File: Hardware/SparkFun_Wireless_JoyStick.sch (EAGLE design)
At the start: 75 parts, among them J7 CORTEX_DEBUGPTH, Q1 2.5A/30V, U1 JOYSTICKPTH, U2 JOYSTICKPTH, U3 74AHC1G125, U4 AP2112K-3.3V, U5 XBEE-2B3, U6 MAX1704X, U7 MCP73831, U8 ATSAMD21G-A, Y1 32.768kHz

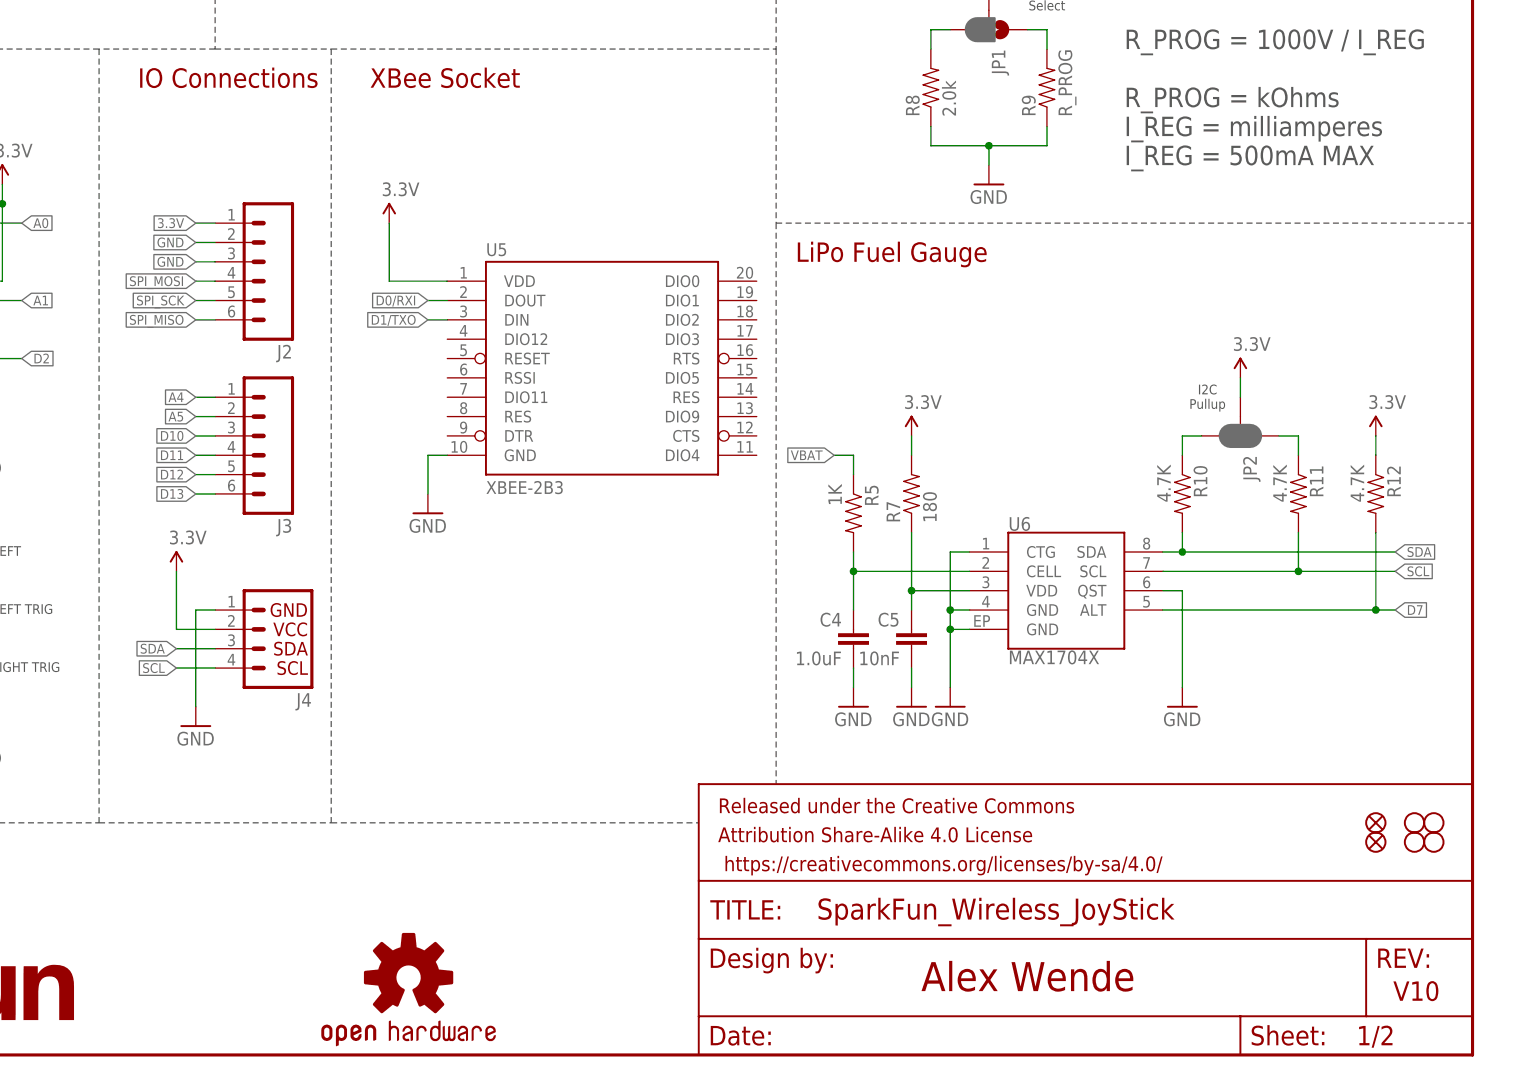
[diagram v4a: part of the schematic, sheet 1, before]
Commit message: QC Issues Fixed
- TX_LED and RX_LED nets are now all 0.006" width
- Version number changed to v01
- IO connections use 3.3V and GND symbols instead of net labels
- Replaced VBAT net label in LiPo Fuel Gauge with PWR symbol
- Inductor PROD_ID updated to match SKU in Sparkle
- Moved JTAG test points to bottom copper
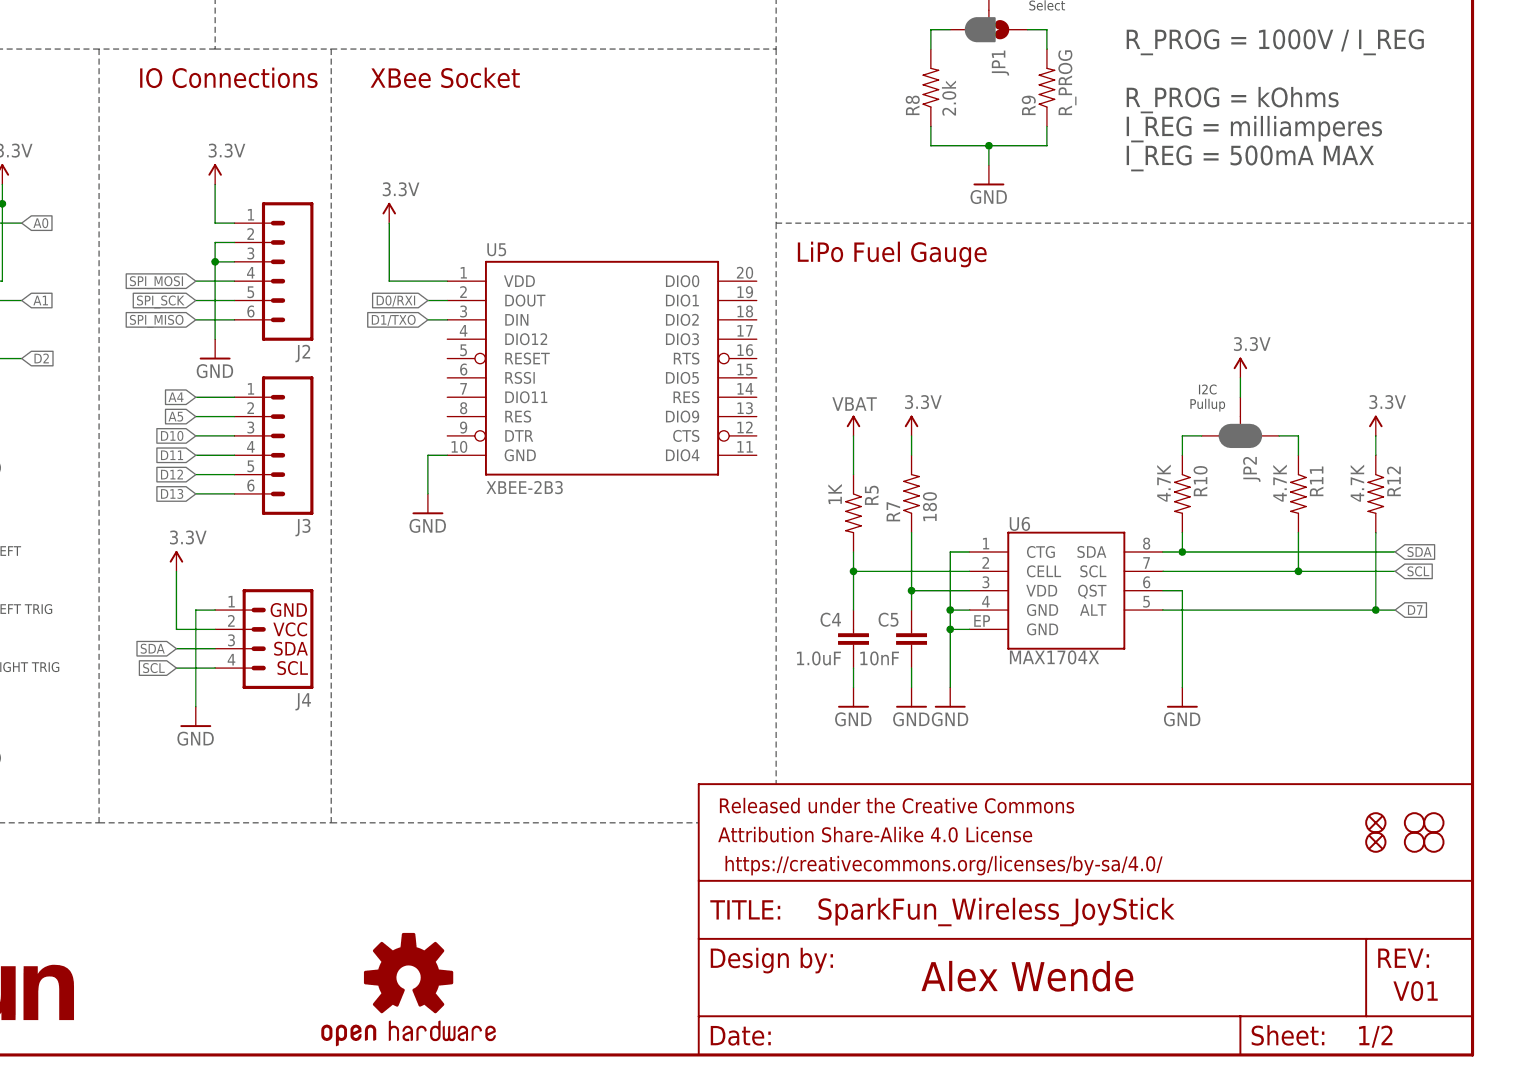
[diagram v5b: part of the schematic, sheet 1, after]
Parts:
- L1: PROD_ID (none) -> NDUC-07859
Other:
- note added: "V01"
- note removed: "V10"
- moved on the sheet: J2, J3
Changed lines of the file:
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@@
 <?xml version="1.0" encoding="utf-8"?>
 <!DOCTYPE eagle SYSTEM "eagle.dtd">
-<eagle version="7.5.0">
+<eagle version="7.6.0">
 <drawing>
 <settings>
@@
 <part name="GND24" library="SparkFun-Aesthetics" deviceset="GND" device=""/>
 <part name="GND23" library="SparkFun-Aesthetics" deviceset="GND" device=""/>
-<part name="L1" library="SparkFun-Passives" deviceset="INDUCTOR" device="30OHM,1.8A" value="FB - 30 Ohm"/>
+<part name="L1" library="SparkFun-Passives" deviceset="INDUCTOR" device="30OHM,1.8A" value="FB - 30 Ohm">
+<attribute name="PROD_ID" value="NDUC-07859"/>
+</part>
 <part name="C7" library="SparkFun-Capacitors" deviceset="0.1UF-25V(+80/-20%)(0603)" device="" value="0.1uF"/>
 <part name="GND21" library="SparkFun-Aesthetics" deviceset="GND" device=""/>
@@
 <part name="R16" library="SparkFun-Resistors" deviceset="470OHM1/10W1%(0603)" device="" value="470"/>
 <part name="GND28" library="SparkFun-Aesthetics" deviceset="GND" device=""/>
+<part name="SUPPLY21" library="SparkFun-Aesthetics" deviceset="3.3V" device=""/>
+<part name="GND29" library="SparkFun-Aesthetics" deviceset="GND" device=""/>
+<part name="SUPPLY22" library="SparkFun-Aesthetics" deviceset="12V" device="" value="VBAT"/>
 </parts>
 <sheets>
@@
 <text x="160.02" y="104.14" size="2.54" layer="94">LiPo Fuel Gauge</text>
 <text x="176.53" y="8.382" size="3.81" layer="94" font="vector">Alex Wende</text>
-<text x="238.506" y="7.112" size="2.54" layer="94" font="vector">V10</text>
+<text x="238.506" y="7.112" size="2.54" layer="94" font="vector">V01</text>
 <wire x1="157.48" y1="185.42" x2="157.48" y2="132.08" width="0.1524" layer="97" style="shortdash"/>
 <wire x1="157.48" y1="132.08" x2="157.48" y2="109.22" width="0.1524" layer="97" style="shortdash"/>
@@
 <instance part="GND7" gate="1" x="81.28" y="43.18"/>
 <instance part="SUPPLY6" gate="G$1" x="78.74" y="63.5"/>
-<instance part="J3" gate="G$1" x="88.9" y="81.28" rot="R180"/>
-<instance part="J2" gate="G$1" x="88.9" y="104.14" rot="R180"/>
+<instance part="J3" gate="G$1" x="91.44" y="81.28" rot="R180"/>
+<instance part="J2" gate="G$1" x="91.44" y="104.14" rot="R180"/>
 <instance part="U7" gate="G$1" x="198.12" y="165.1"/>
 <instance part="D2" gate="G$1" x="177.8" y="152.4" rot="MR270"/>
@@
 <instance part="SUPPLY8" gate="G$1" x="106.68" y="109.22"/>
 <instance part="GND9" gate="1" x="111.76" y="71.12"/>
+<instance part="SUPPLY21" gate="G$1" x="83.82" y="114.3"/>
+<instance part="GND29" gate="1" x="83.82" y="91.44"/>
+<instance part="SUPPLY22" gate="G$1" x="167.64" y="81.28" smashed="yes">
+<attribute name="VALUE" x="164.846" y="84.582" size="1.778" layer="96"/>
+</instance>
 </instances>
 <busses>
@@
 </segment>
 <segment>
+<pinref part="J2" gate="G$1" pin="2"/>
+<wire x1="86.36" y1="106.68" x2="83.82" y2="106.68" width="0.1524" layer="91"/>
 <pinref part="J2" gate="G$1" pin="3"/>
-<wire x1="83.82" y1="104.14" x2="81.28" y2="104.14" width="0.1524" layer="91"/>
-<label x="81.28" y="104.14" size="1.27" layer="95" rot="R180" xref="yes"/>
-</segment>
-<segment>
-<pinref part="J2" gate="G$1" pin="2"/>
-<wire x1="83.82" y1="106.68" x2="81.28" y2="106.68" width="0.1524" layer="91"/>
-<label x="81.28" y="106.68" size="1.27" layer="95" rot="R180" xref="yes"/>
+<wire x1="86.36" y1="104.14" x2="83.82" y2="104.14" width="0.1524" layer="91"/>
+<wire x1="83.82" y1="106.68" x2="83.82" y2="104.14" width="0.1524" layer="91"/>
+<pinref part="GND29" gate="1" pin="GND"/>
+<wire x1="83.82" y1="104.14" x2="83.82" y2="93.98" width="0.1524" layer="91"/>
+<junction x="83.82" y="104.14"/>
 </segment>
 <segment>
@@
 <segment>
 <pinref part="J2" gate="G$1" pin="1"/>
-<wire x1="83.82" y1="109.22" x2="81.28" y2="109.22" width="0.1524" layer="91"/>
-<label x="81.28" y="109.22" size="1.27" layer="95" rot="R180" xref="yes"/>
+<wire x1="86.36" y1="109.22" x2="83.82" y2="109.22" width="0.1524" layer="91"/>
+<pinref part="SUPPLY21" gate="G$1" pin="3.3V"/>
+<wire x1="83.82" y1="109.22" x2="83.82" y2="114.3" width="0.1524" layer="91"/>
 </segment>
 <segment>
@@
 <label x="81.28" y="78.74" size="1.27" layer="95" rot="R180" xref="yes"/>
 <pinref part="J3" gate="G$1" pin="4"/>
-<wire x1="81.28" y1="78.74" x2="83.82" y2="78.74" width="0.1524" layer="91"/>
+<wire x1="81.28" y1="78.74" x2="86.36" y2="78.74" width="0.1524" layer="91"/>
 </segment>
 </net>
@@
 <label x="81.28" y="76.2" size="1.27" layer="95" rot="R180" xref="yes"/>
 <pinref part="J3" gate="G$1" pin="5"/>
-<wire x1="81.28" y1="76.2" x2="83.82" y2="76.2" width="0.1524" layer="91"/>
+<wire x1="81.28" y1="76.2" x2="86.36" y2="76.2" width="0.1524" layer="91"/>
 </segment>
 </net>
@@
 <segment>
 <pinref part="J2" gate="G$1" pin="4"/>
-<wire x1="83.82" y1="101.6" x2="81.28" y2="101.6" width="0.1524" layer="91"/>
+<wire x1="86.36" y1="101.6" x2="81.28" y2="101.6" width="0.1524" layer="91"/>
 <label x="81.28" y="101.6" size="1.27" layer="95" rot="R180" xref="yes"/>
 </segment>
@@
 <segment>
 <pinref part="J2" gate="G$1" pin="5"/>
-<wire x1="83.82" y1="99.06" x2="81.28" y2="99.06" width="0.1524" layer="91"/>
+<wire x1="86.36" y1="99.06" x2="81.28" y2="99.06" width="0.1524" layer="91"/>
 <label x="81.28" y="99.06" size="1.27" layer="95" rot="R180" xref="yes"/>
 </segment>
@@
 <segment>
 <pinref part="J2" gate="G$1" pin="6"/>
-<wire x1="83.82" y1="96.52" x2="81.28" y2="96.52" width="0.1524" layer="91"/>
+<wire x1="86.36" y1="96.52" x2="81.28" y2="96.52" width="0.1524" layer="91"/>
 <label x="81.28" y="96.52" size="1.27" layer="95" rot="R180" xref="yes"/>
 </segment>
@@
 <label x="81.28" y="73.66" size="1.27" layer="95" rot="R180" xref="yes"/>
 <pinref part="J3" gate="G$1" pin="6"/>
-<wire x1="81.28" y1="73.66" x2="83.82" y2="73.66" width="0.1524" layer="91"/>
+<wire x1="81.28" y1="73.66" x2="86.36" y2="73.66" width="0.1524" layer="91"/>
 </segment>
 </net>
@@
 <label x="81.28" y="81.28" size="1.27" layer="95" rot="R180" xref="yes"/>
 <pinref part="J3" gate="G$1" pin="3"/>
-<wire x1="81.28" y1="81.28" x2="83.82" y2="81.28" width="0.1524" layer="91"/>
+<wire x1="81.28" y1="81.28" x2="86.36" y2="81.28" width="0.1524" layer="91"/>
 </segment>
 </net>
@@
 <label x="81.28" y="86.36" size="1.27" layer="95" rot="R180" xref="yes"/>
 <pinref part="J3" gate="G$1" pin="1"/>
-<wire x1="83.82" y1="86.36" x2="81.28" y2="86.36" width="0.1524" layer="91"/>
+<wire x1="86.36" y1="86.36" x2="81.28" y2="86.36" width="0.1524" layer="91"/>
 </segment>
 </net>
@@
 <label x="81.28" y="83.82" size="1.27" layer="95" rot="R180" xref="yes"/>
 <pinref part="J3" gate="G$1" pin="2"/>
-<wire x1="83.82" y1="83.82" x2="81.28" y2="83.82" width="0.1524" layer="91"/>
+<wire x1="86.36" y1="83.82" x2="81.28" y2="83.82" width="0.1524" layer="91"/>
 </segment>
 </net>
@@
 </segment>
 <segment>
+<pinref part="SUPPLY22" gate="G$1" pin="12V"/>
 <pinref part="R5" gate="G$1" pin="1"/>
-<wire x1="167.64" y1="76.2" x2="167.64" y2="78.74" width="0.1524" layer="91"/>
-<wire x1="167.64" y1="78.74" x2="165.1" y2="78.74" width="0.1524" layer="91"/>
-<label x="165.1" y="78.74" size="1.27" layer="95" rot="R180" xref="yes"/>
+<wire x1="167.64" y1="81.28" x2="167.64" y2="76.2" width="0.1524" layer="91"/>
 </segment>
 </net>
@@
 <plain>
 <text x="173.99" y="8.382" size="3.81" layer="94" font="vector">Alex Wende</text>
-<text x="238.506" y="7.112" size="2.54" layer="94" font="vector">V10</text>
+<text x="238.506" y="7.112" size="2.54" layer="94" font="vector">V01</text>
 <text x="5.08" y="180.34" size="2.54" layer="94">SAMD21</text>
 <text x="149.86" y="180.34" size="2.54" layer="94">JTAG Programmer</text>
@@
 <segment>
 <pinref part="R15" gate="G$1" pin="1"/>
-<wire x1="190.5" y1="50.8" x2="190.5" y2="45.72" width="0.2032" layer="91"/>
-<wire x1="190.5" y1="45.72" x2="177.8" y2="45.72" width="0.2032" layer="91"/>
+<wire x1="190.5" y1="50.8" x2="190.5" y2="45.72" width="0.1524" layer="91"/>
+<wire x1="190.5" y1="45.72" x2="177.8" y2="45.72" width="0.1524" layer="91"/>
 <label x="177.8" y="45.72" size="1.27" layer="95" rot="R180" xref="yes"/>
 </segment>
@@
 <segment>
 <pinref part="R14" gate="G$1" pin="1"/>
-<wire x1="180.34" y1="50.8" x2="180.34" y2="48.26" width="0.2032" layer="91"/>
-<wire x1="180.34" y1="48.26" x2="177.8" y2="48.26" width="0.2032" layer="91"/>
+<wire x1="180.34" y1="50.8" x2="180.34" y2="48.26" width="0.1524" layer="91"/>
+<wire x1="180.34" y1="48.26" x2="177.8" y2="48.26" width="0.1524" layer="91"/>
 <label x="177.8" y="48.26" size="1.27" layer="95" rot="R180" xref="yes"/>
 </segment>

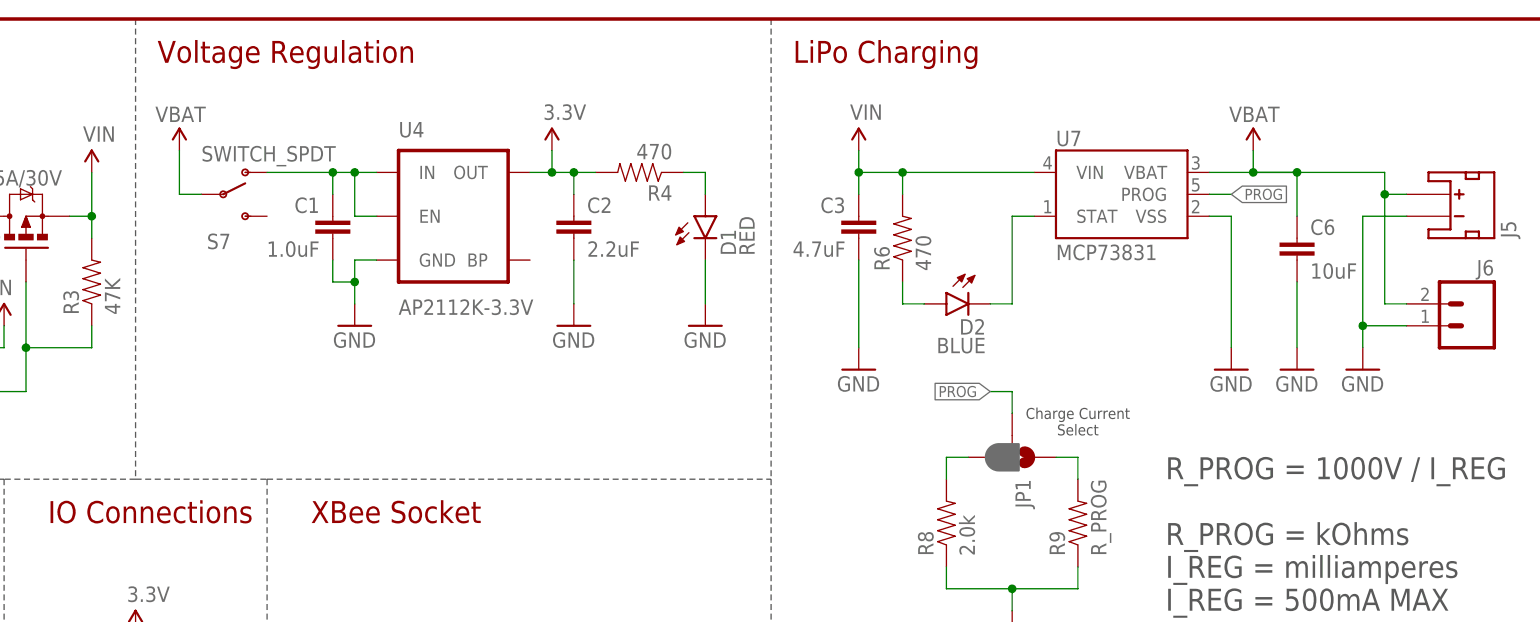
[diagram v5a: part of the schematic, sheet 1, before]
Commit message: Proto Changes
- Added diode to allow powering the board from USB when no battery is
present.
- Switch now controls enable pin instead of VCC rail
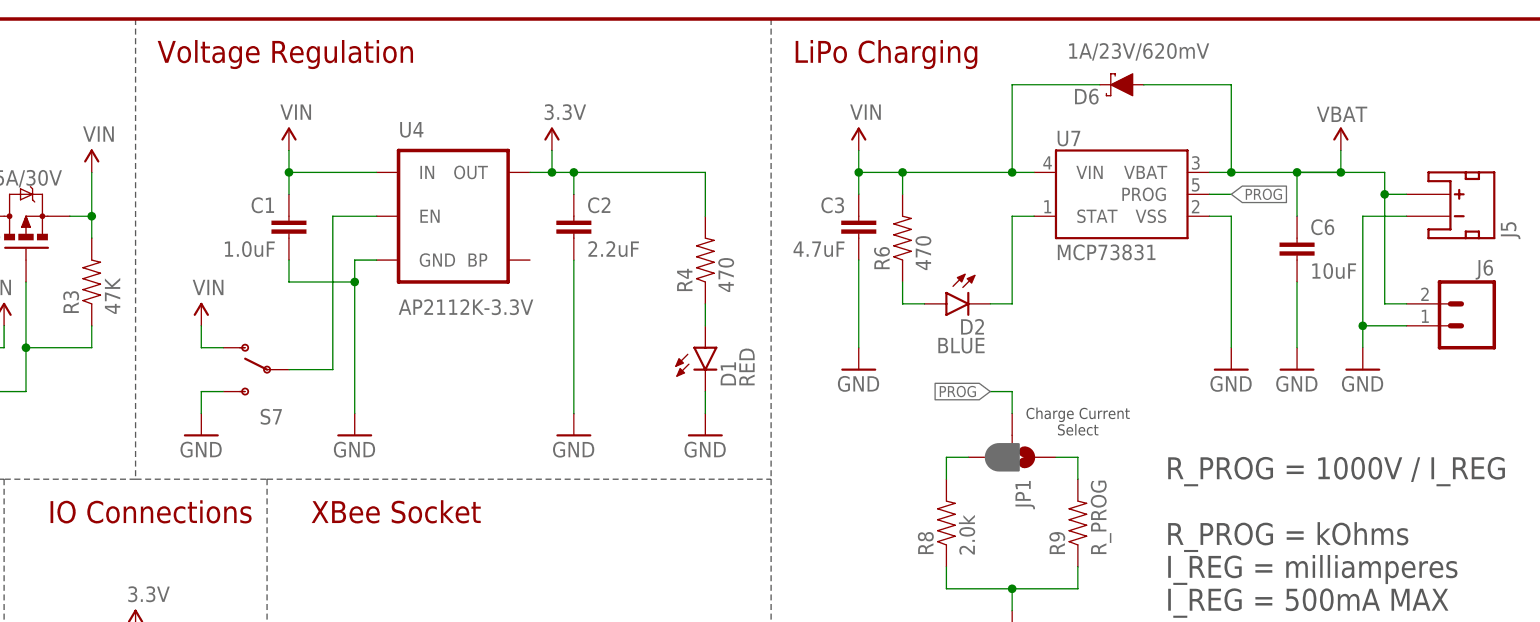
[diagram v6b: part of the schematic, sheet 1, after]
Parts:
- added D6: 1A/23V/620mV, SparkFun-DiscreteSemi:DIODE-SCHOTTKY-BAT20J
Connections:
- removed net VBAT_SW: C1.1, S7.O, U4.EN, U4.IN
- new net N$13: S7.P, U4.EN
- net GND: now also S7.S
- net VBAT: now also D6.A; no longer S7.P
- net VIN: now also C1.1, D6.C, S7.O, U4.IN
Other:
- moved on the sheet: C1, D1, R4, S7

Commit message: Updating version to 10
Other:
- note added: "V10"
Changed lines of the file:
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@@
 <text x="160.02" y="104.14" size="2.54" layer="94">LiPo Fuel Gauge</text>
 <text x="176.53" y="8.382" size="3.81" layer="94" font="vector">Alex Wende</text>
-<text x="238.506" y="7.112" size="2.54" layer="94" font="vector">V01</text>
+<text x="238.506" y="7.112" size="2.54" layer="94" font="vector">V10</text>
 <wire x1="157.48" y1="185.42" x2="157.48" y2="132.08" width="0.1524" layer="97" style="shortdash"/>
 <wire x1="157.48" y1="132.08" x2="157.48" y2="109.22" width="0.1524" layer="97" style="shortdash"/>

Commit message: Updating to version 10
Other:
- note removed: "V01"
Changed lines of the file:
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@@
 <plain>
 <text x="173.99" y="8.382" size="3.81" layer="94" font="vector">Alex Wende</text>
-<text x="238.506" y="7.112" size="2.54" layer="94" font="vector">V01</text>
+<text x="238.506" y="7.112" size="2.54" layer="94" font="vector">V10</text>
 <text x="5.08" y="180.34" size="2.54" layer="94">SAMD21</text>
 <text x="149.86" y="180.34" size="2.54" layer="94">JTAG Programmer</text>
